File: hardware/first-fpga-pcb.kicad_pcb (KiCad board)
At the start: 2 copper layers, 100 x 70 mm, 74 parts, among them J1 Conn_01x02, J2 Conn_01x08, J3 Conn_02x06_Odd_Even, J4 Conn_02x06_Odd_Even, J5 Conn_02x06_Odd_Even, J6 Conn_02x06_Odd_Even, J7 Conn_02x06_Odd_Even, J8 Conn_02x06_Odd_Even, J9 Conn_02x20_Odd_Even, Q1 Q_NMOS_GSD, SW1 SW_Push, SW2 SW_Push, U1 iCE40-HX4K-TQ144, U2 IS25LP016D-JBLE, U3 TLV73312PDBV, U4 TLV73333PDBV, X1 SiT2001B

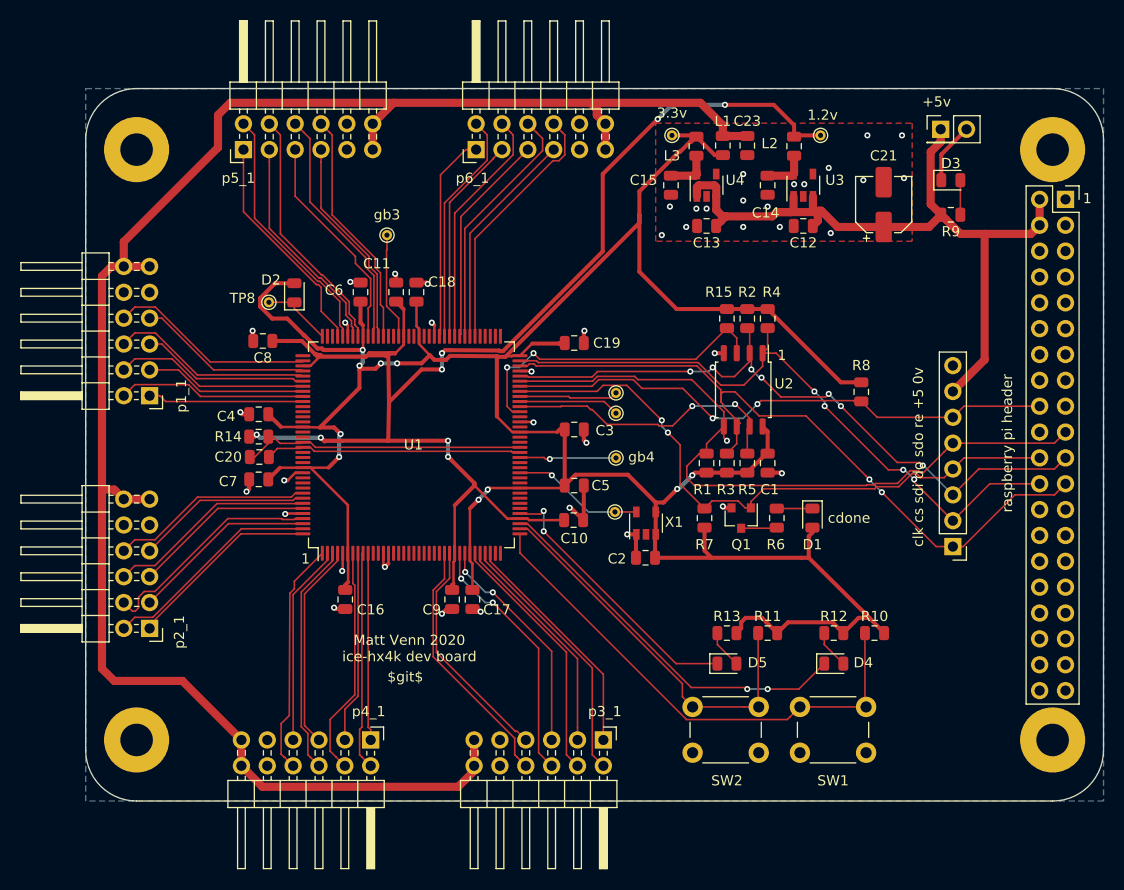
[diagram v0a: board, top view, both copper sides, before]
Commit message: fixed a few things and added features as detailed in README.md
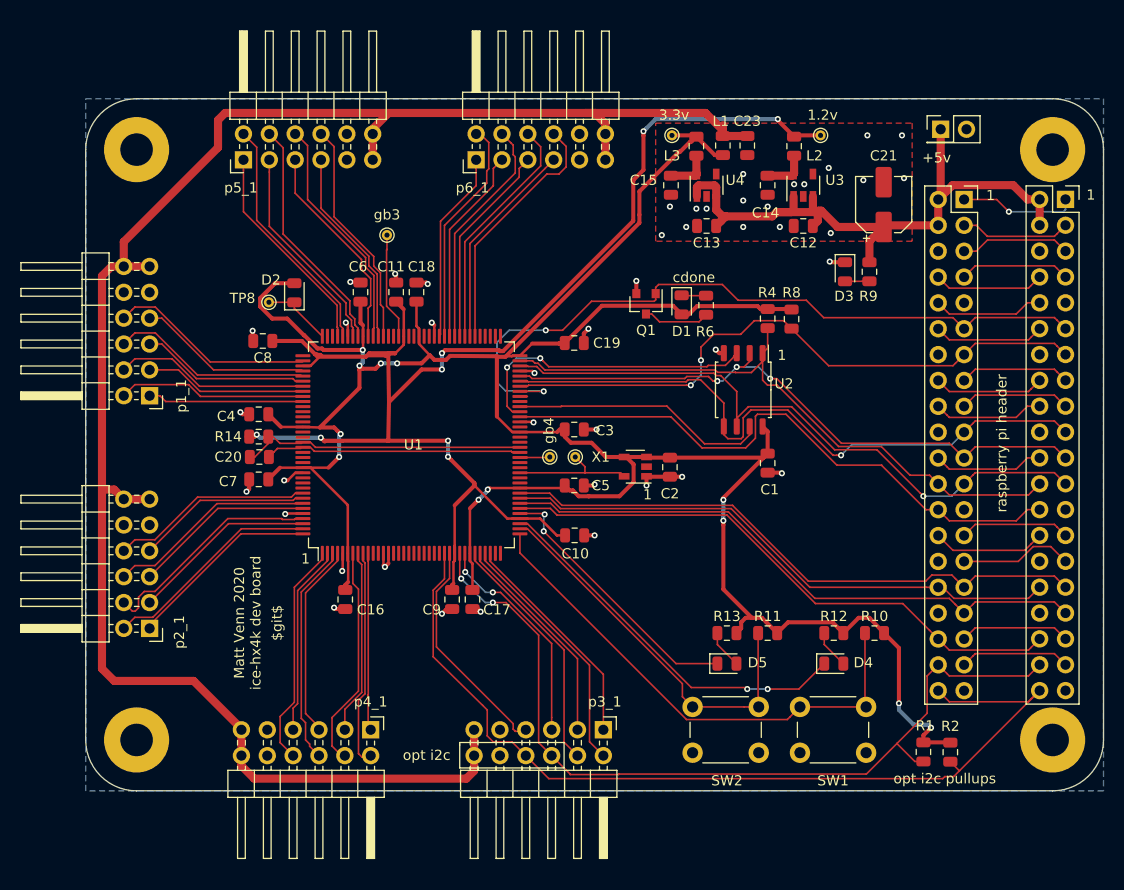
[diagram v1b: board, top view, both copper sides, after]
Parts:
- removed R15, R3, R5, R7: dnp, Resistor_SMD:R_0805_2012Metric
- removed TP3: cbsel0, TestPoint:TestPoint_THTPad_D1.0mm_Drill0.5mm
- removed TP4: cbsel1, TestPoint:TestPoint_THTPad_D1.0mm_Drill0.5mm
- J2: value Conn_01x08 -> Conn_02x20_Odd_Even; footprint Connector_PinHeader_2.54mm:PinHeader_1x08_P2.54mm_Vertical -> Connector_PinSocket_2.54mm:PinSocket_2x20_P2.54mm_Vertical
- R1, R2: value dnp -> 10k
- moved R2 47.0 mm to (159.9, 115.2), turned to 270 degrees
- moved R1 35.5 mm to (157.3, 115.2)
- moved J2 34.1 mm to (161.3, 60.9), turned to 0 degrees
- moved D1 24.6 mm to (133.6, 71.2)
- moved Q1 23.0 mm to (130.1, 71.2)
- moved R6 22.0 mm to (135.9, 71.3)
- moved D3 13.8 mm to (149.6, 68.0), turned to 270 degrees
- moved R8 9.90 mm to (144.3, 72.7)
- moved R9 9.77 mm to (152.0, 68.0), turned to 90 degrees
- moved C2 9.22 mm to (132.4, 87.2), turned to 270 degrees
- moved TP5 6.66 mm to (123.1, 86.2), turned to 270 degrees
- moved TP2 6.50 mm to (120.6, 86.2)
- moved X1 5.65 mm to (129.0, 87.2), turned to 180 degrees
- moved C10 1.50 mm to (123.0, 93.9)
- moved J5 1.00 mm to (125.9, 113.0)
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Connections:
- J2 pad 1: /sd_clk -> /pi_3v3
- J2 pad 2: /sd_cs -> +5V
- J2 pad 3: /sdi -> /gp2
- J2 pad 4: /cdone -> +5V
- J2 pad 5: /sdo -> /gp3
- J2 pad 6: /creset -> GND
- J2 pad 7: +5V -> /gp4
- J2 pad 8: GND -> /gp14
- J5 pad 6: /p3_9 -> /gp20
- J5 pad 8: /p3_10 -> /gp21
- J9 pad 1: Net-(J9-Pad1) -> /pi_3v3
- J9 pad 10: Net-(J9-Pad10) -> /gp15
- J9 pad 11: Net-(J9-Pad11) -> /cdone
- J9 pad 12: Net-(J9-Pad12) -> /gp18
- J9 pad 13: Net-(J9-Pad13) -> /creset
- J9 pad 14: Net-(J9-Pad14) -> GND
- J9 pad 15: Net-(J9-Pad15) -> /gp22
- J9 pad 16: Net-(J9-Pad16) -> /gp23
- J9 pad 17: Net-(J9-Pad17) -> /pi_3v3_2
- J9 pad 18: /creset -> /gp24
- J9 pad 19: /sdo -> /gp10
- J9 pad 21: /sdi -> /gp9
- J9 pad 22: /cdone -> /gp25
- J9 pad 23: /sd_clk -> /gp11
- J9 pad 24: /sd_cs -> /gp8
- J9 pad 26: Net-(J9-Pad26) -> /ce1
- J9 pad 27: Net-(J9-Pad27) -> /gp0
- J9 pad 28: Net-(J9-Pad28) -> /gp1
- J9 pad 29: Net-(J9-Pad29) -> /gp5
- J9 pad 3: Net-(J9-Pad3) -> /gp2
- J9 pad 30: Net-(J9-Pad30) -> GND
- J9 pad 31: Net-(J9-Pad31) -> /gp6
- J9 pad 32: Net-(J9-Pad32) -> /gp12
- J9 pad 33: Net-(J9-Pad33) -> /gp13
- J9 pad 34: Net-(J9-Pad34) -> GND
- J9 pad 35: Net-(J9-Pad35) -> /gp19
- J9 pad 36: Net-(J9-Pad36) -> /gp16
- J9 pad 37: Net-(J9-Pad37) -> /gp26
- J9 pad 38: Net-(J9-Pad38) -> /gp20
- J9 pad 39: Net-(J9-Pad39) -> GND
- J9 pad 40: Net-(J9-Pad40) -> /gp21
- J9 pad 5: Net-(J9-Pad5) -> /gp3
- J9 pad 7: Net-(J9-Pad7) -> /gp4
- J9 pad 8: Net-(J9-Pad8) -> /gp14
- J9 pad 9: Net-(J9-Pad9) -> GND
- R1 pad 1: /sdo -> +3V3
- R1 pad 2: +3V3 -> /gp20
- R2 pad 1: /sdi -> +3V3
- R2 pad 2: +3V3 -> /gp21
- R4 pad 1: /sd_cs -> +3V3
- R4 pad 2: +3V3 -> /gp8
- U1 pad 25: /p3_10 -> /gp21
- U1 pad 28: /p3_9 -> /gp20
- U1 pad 42: Net-(U1-Pad42) -> /gp16
- U1 pad 43: Net-(U1-Pad43) -> /gp13
- U1 pad 44: Net-(U1-Pad44) -> /gp12
- U1 pad 45: Net-(U1-Pad45) -> /gp6
- U1 pad 60: Net-(U1-Pad60) -> /ce1
- U1 pad 67: /sdo -> /gp10
- U1 pad 68: /sdi -> /gp9
- U1 pad 70: /sd_clk -> /gp11
- U1 pad 71: /sd_cs -> /gp8
- U2 pad 1: /sd_cs -> /gp8
- U2 pad 2: /sdi -> /gp9
- U2 pad 5: /sdo -> /gp10
- U2 pad 6: /sd_clk -> /gp11
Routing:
- net /gp21: track 0.00 -> 92.4 mm
- net /gp20: track 0.00 -> 84.4 mm, vias 0 -> 2
- net /sd_clk: track 72.0 -> 0.00 mm, vias 2 -> 0
- net /sdo: track 71.5 -> 0.00 mm, vias 1 -> 0
- net /sdi: track 66.7 -> 0.00 mm, vias 7 -> 0
- net /sd_cs: track 65.5 -> 0.00 mm, vias 4 -> 0
- net /gp11: track 0.00 -> 64.4 mm, vias 0 -> 1
- net /gp10: track 0.00 -> 63.9 mm, vias 0 -> 1
- net /gp8: track 0.00 -> 62.4 mm
- net /gp9: track 0.00 -> 61.5 mm, vias 0 -> 3
- net /ce1: track 0.00 -> 59.8 mm
- net /gp13: track 0.00 -> 59.0 mm
- net /gp6: track 0.00 -> 58.8 mm
- net /gp16: track 0.00 -> 57.3 mm
- net /gp12: track 0.00 -> 55.6 mm
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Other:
- board size 100 x 70 mm -> 100 x 68 mm
- board text added: "2 approved DRC errors"
- board text added: "opt i2c"
- board text added: "opt i2c pullups"
- board text removed: "clk cs sdi do sdo re +5 0v"

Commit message: change pmod to female
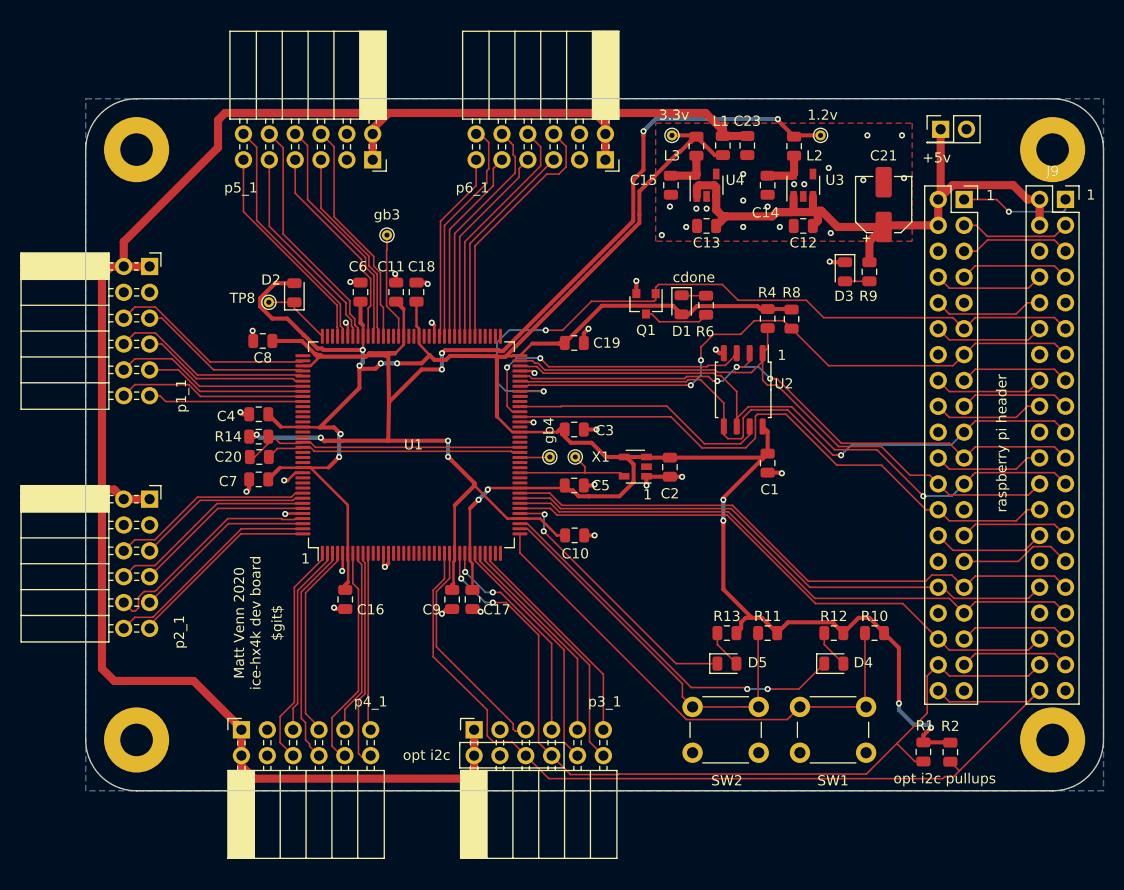
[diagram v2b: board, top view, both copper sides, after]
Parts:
- J3, J4, J5, J6, J7, J8: footprint Connector_PinHeader_2.54mm:PinHeader_2x06_P2.54mm_Horizontal -> Connector_PinSocket_2.54mm:PinSocket_2x06_P2.54mm_Horizontal
- moved J3 12.7 mm to (81.3, 67.5), turned to 0 degrees
- moved J4 12.7 mm to (81.3, 90.3), turned to 0 degrees
- moved J5 12.7 mm to (113.2, 113.0), turned to 90 degrees
- moved J6 12.7 mm to (90.3, 113.0), turned to 90 degrees
- moved J7 12.7 mm to (103.2, 57.0), turned to 270 degrees
- moved J8 12.7 mm to (126.1, 57.0), turned to 270 degrees
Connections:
- J3 pad 1: /p1_1 -> +3.3VP
- J3 pad 10: GND -> /p1_8
- J3 pad 11: +3.3VP -> /p1_1
- J3 pad 12: +3.3VP -> /p1_7
- J3 pad 2: /p1_7 -> +3.3VP
- J3 pad 3: /p1_2 -> GND
- J3 pad 4: /p1_8 -> GND
- J3 pad 5: /p1_3 -> /p1_4
- J3 pad 6: /p1_9 -> /p1_10
- J3 pad 7: /p1_4 -> /p1_3
- J3 pad 8: /p1_10 -> /p1_9
- J3 pad 9: GND -> /p1_2
- J4 pad 1: /p2_1 -> +3.3VP
- J4 pad 10: GND -> /p2_8
- J4 pad 11: +3.3VP -> /p2_1
- J4 pad 12: +3.3VP -> /p2_7
- J4 pad 2: /p2_7 -> +3.3VP
- J4 pad 3: /p2_2 -> GND
- J4 pad 4: /p2_8 -> GND
- J4 pad 5: /p2_3 -> /p2_4
- J4 pad 6: /p2_9 -> /p2_10
- J4 pad 7: /p2_4 -> /p2_3
- J4 pad 8: /p2_10 -> /p2_9
- J4 pad 9: GND -> /p2_2
- J5 pad 1: /p3_1 -> +3.3VP
- J5 pad 10: GND -> /p3_8
- J5 pad 11: +3.3VP -> /p3_1
- J5 pad 12: +3.3VP -> /p3_7
- J5 pad 2: /p3_7 -> +3.3VP
- J5 pad 3: /p3_2 -> GND
- J5 pad 4: /p3_8 -> GND
- J5 pad 5: /p3_3 -> /p3_4
- J5 pad 6: /gp20 -> /gp21
- J5 pad 7: /p3_4 -> /p3_3
- J5 pad 8: /gp21 -> /gp20
- J5 pad 9: GND -> /p3_2
- J6 pad 1: /p4_1 -> +3.3VP
- J6 pad 10: GND -> /p4_8
- J6 pad 11: +3.3VP -> /p4_1
- J6 pad 12: +3.3VP -> /p4_7
- J6 pad 2: /p4_7 -> +3.3VP
- J6 pad 3: /p4_2 -> GND
- J6 pad 4: /p4_8 -> GND
- J6 pad 5: /p4_3 -> /p4_4
- J6 pad 6: /p4_9 -> /p4_10
- J6 pad 7: /p4_4 -> /p4_3
- J6 pad 8: /p4_10 -> /p4_9
- J6 pad 9: GND -> /p4_2
- J7 pad 1: /p5_1 -> +3.3VP
- J7 pad 10: GND -> /p5_8
- J7 pad 11: +3.3VP -> /p5_1
- J7 pad 12: +3.3VP -> /p5_7
- J7 pad 2: /p5_7 -> +3.3VP
- J7 pad 3: /p5_2 -> GND
- J7 pad 4: /p5_8 -> GND
- J7 pad 5: /p5_3 -> /p5_4
- J7 pad 6: /p5_9 -> /p5_10
- J7 pad 7: /p5_4 -> /p5_3
- J7 pad 8: /p5_10 -> /p5_9
- J7 pad 9: GND -> /p5_2
- J8 pad 1: /p6_1 -> +3.3VP
- J8 pad 10: GND -> /p6_8
- J8 pad 11: +3.3VP -> /p6_1
- J8 pad 12: +3.3VP -> /p6_7
- J8 pad 2: /p6_7 -> +3.3VP
- J8 pad 3: /p6_2 -> GND
- J8 pad 4: /p6_8 -> GND
- J8 pad 5: /p6_3 -> /p6_4
- J8 pad 6: /p6_9 -> /p6_10
- J8 pad 7: /p6_4 -> /p6_3
- J8 pad 8: /p6_10 -> /p6_9
- J8 pad 9: GND -> /p6_2

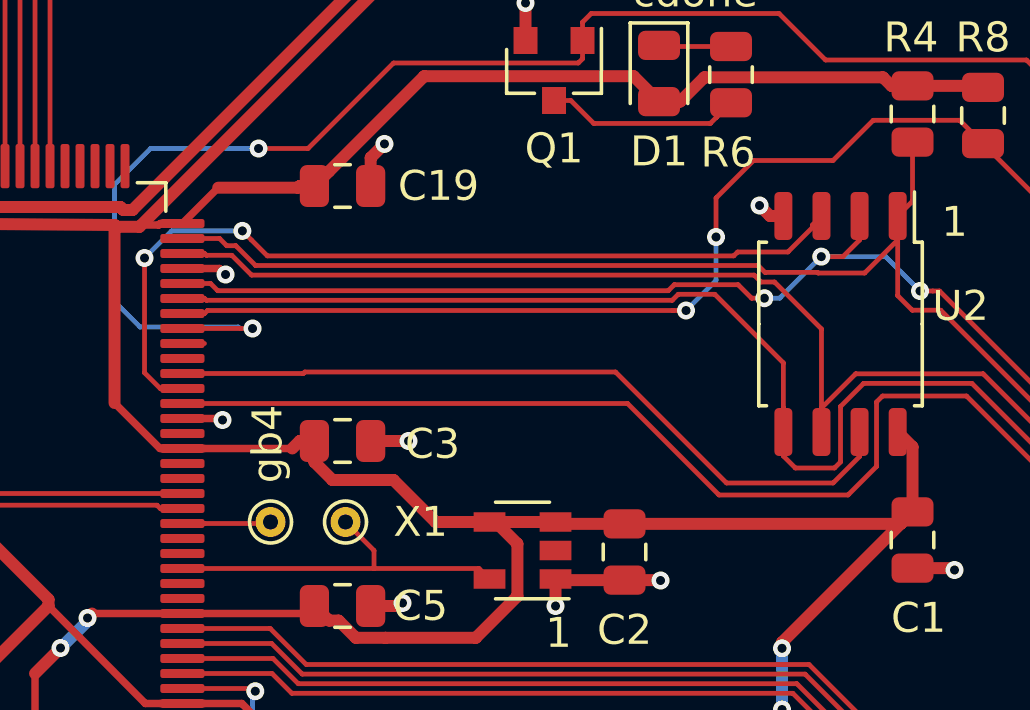
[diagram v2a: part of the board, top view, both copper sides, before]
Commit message: fixed missing hold resistor
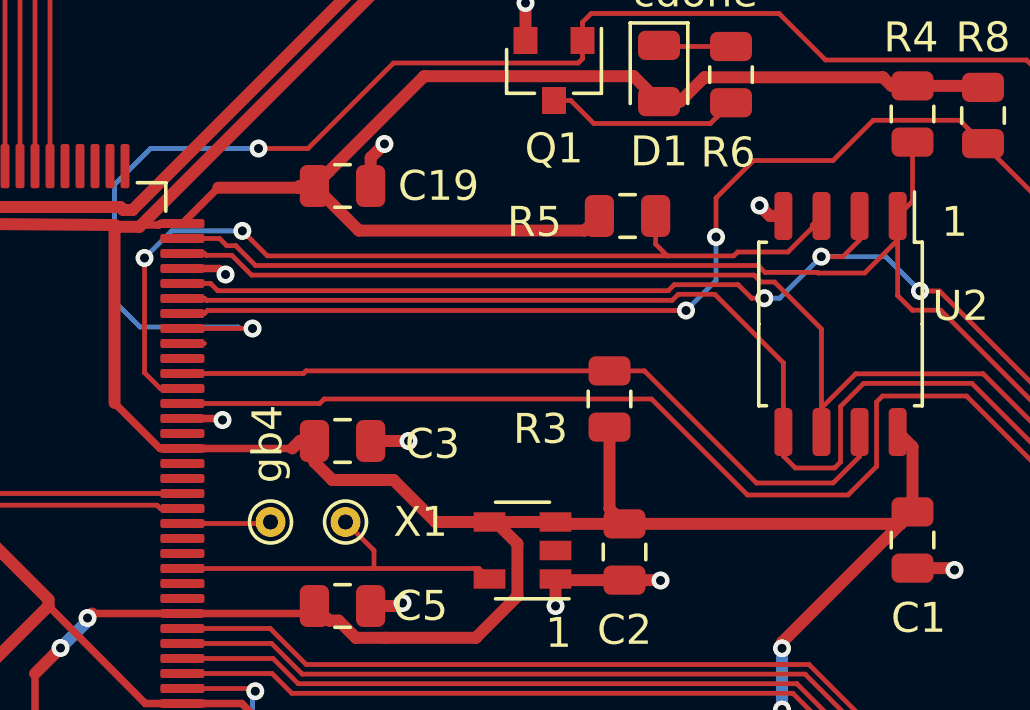
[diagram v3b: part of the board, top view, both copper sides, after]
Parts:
- added R3: 10k, Resistor_SMD:R_0805_2012Metric, F.Cu at (131.9, 82.1)
- added R5: 10k, Resistor_SMD:R_0805_2012Metric, F.Cu at (132.5, 76.0)
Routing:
- net +3V3: track 275.5 -> 289.3 mm
- net /sd_io2: track 29.2 -> 30.7 mm
